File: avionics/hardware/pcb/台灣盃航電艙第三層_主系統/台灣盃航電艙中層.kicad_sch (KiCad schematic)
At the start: 54 parts, among them J2 Micro_SD_Card_Det2, J3 Conn_01x04_Pin, SW1 SW_SPST, U1 STM32F405VGT6, U2 BMI088, U3 BMP390L, U4 Connector, U5 H3LIS331DL, Y1 8MHz

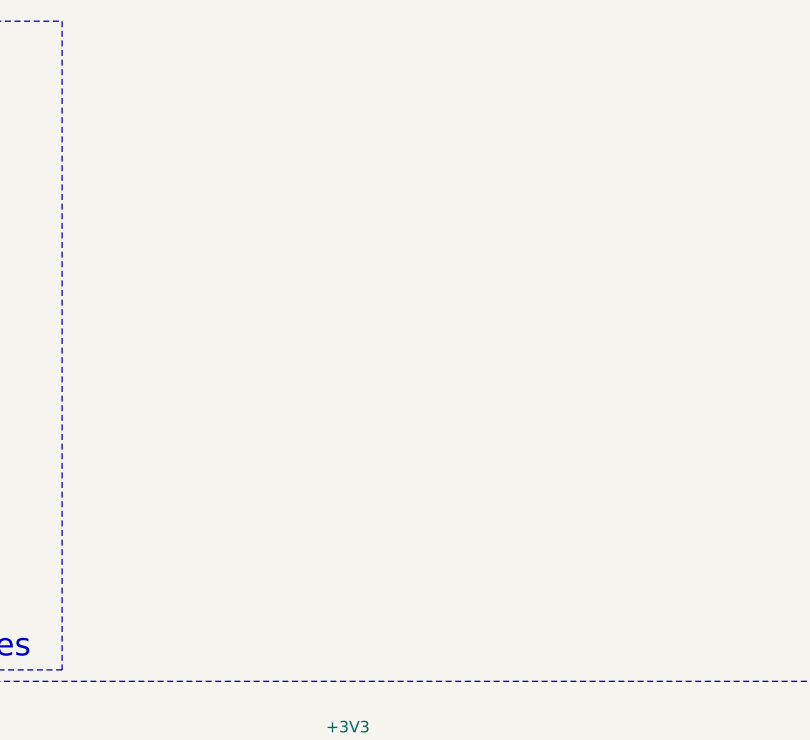
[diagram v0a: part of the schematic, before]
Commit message: 上傳新的連接器
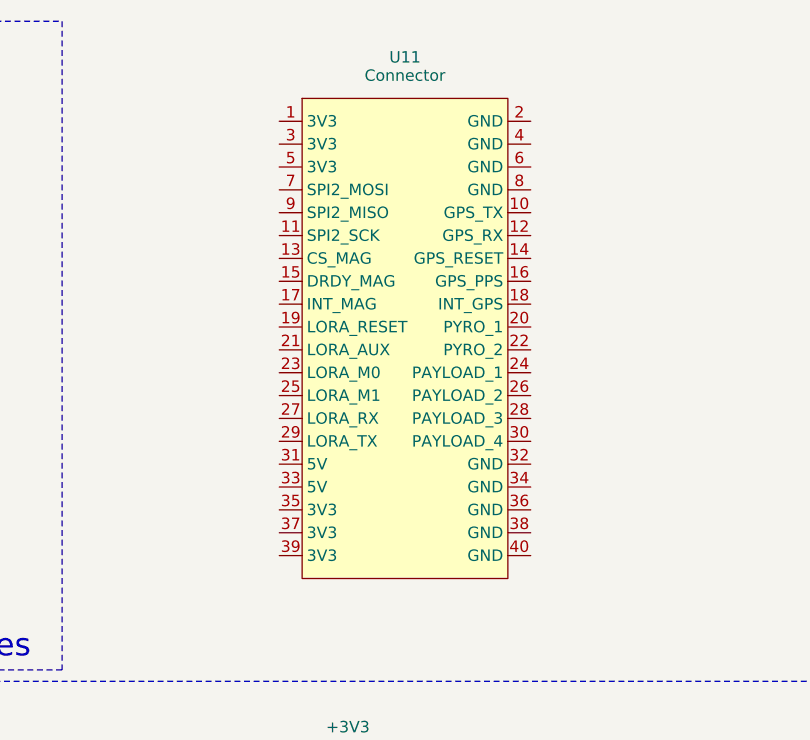
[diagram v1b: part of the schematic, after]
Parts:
- added U11: Connector, symbol MySymbol:2*20 PC104
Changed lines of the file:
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@@
+	)
+	(symbol
+		(lib_id "MySymbol:2*20 PC104")
+		(at 290.83 21.59 0)
+		(unit 1)
+		(exclude_from_sim no)
+		(in_bom yes)
+		(on_board yes)
+		(dnp no)
+		(property "Reference" "U11"
+			(at 290.83 18.288 0)
+			(effects
+				(font
+					(size 1.27 1.27)
+				)
+			)
+		)
+		(property "Value" "Connector"
+			(at 290.83 20.32 0)
+			(effects
+				(font
+					(size 1.27 1.27)
+				)
+			)
+		)
+		(property "Footprint" ""
+			(at 290.83 21.59 0)
+			(effects
+				(font
+					(size 1.27 1.27)
+				)
+				(hide yes)
+			)
+		)
+		(property "Datasheet" ""
+			(at 290.83 21.59 0)
+			(effects
+				(font
+					(size 1.27 1.27)
+				)
+				(hide yes)
+			)
+		)
+		(property "Description" ""
+			(at 290.83 21.59 0)
+			(effects
+				(font
+					(size 1.27 1.27)
+				)
+				(hide yes)
+			)
+		)
+		(pin "19"
+		)
+		(pin "39"
+		)
+		(pin "9"
+		)
+		(pin "15"
+		)
+		(pin "11"
+		)
+		(pin "7"
+		)
+		(pin "29"
+		)
+		(pin "31"
+		)
+		(pin "5"
+		)
+		(pin "4"
+		)
+		(pin "1"
+		)
+		(pin "21"
+		)
+		(pin "12"
+		)
+		(pin "27"
+		)
+		(pin "16"
+		)
+		(pin "20"
+		)
+		(pin "23"
+		)
+		(pin "13"
+		)
+		(pin "17"
+		)
+		(pin "3"
+		)
+		(pin "25"
+		)
+		(pin "33"
+		)
+		(pin "35"
+		)
+		(pin "37"
+		)
+		(pin "6"
+		)
+		(pin "2"
+		)
+		(pin "8"
+		)
+		(pin "14"
+		)
+		(pin "18"
+		)
+		(pin "10"
+		)
+		(pin "24"
+		)
+		(pin "26"
+		)
+		(pin "32"
+		)
+		(pin "34"
+		)
+		(pin "36"
+		)
+		(pin "38"
+		)
+		(pin "28"
+		)
+		(pin "30"
+		)
+		(pin "22"
+		)
+		(pin "40"
+		)
+		(instances
+			(project "台灣盃航電艙中層"
+				(path "/4789330c-02e1-4fa2-9a82-fdad6a603275"
+					(reference "U11")
+					(unit 1)
+				)
+			)
+		)
 	)
 	(symbol

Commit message: 將第一至三層連接器修改成PC104規格，第四層還未進行
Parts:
- removed C23, C26: 10u, Capacitor_SMD:C_0805_2012Metric, symbol Device:C
- removed C24, C27: 100n, Capacitor_SMD:C_0603_1608Metric, symbol Device:C
- removed U4: Connector, Connector_PinHeader_1.00mm:PinHeader_2x17_P1.00mm_Vertical, symbol MySymbol:2x16排針母座連接
- added C30, C32: 100n, Capacitor_SMD:C_0402_1005Metric, symbol Device:C
- added C31, C33: 10u, Capacitor_SMD:C_0603_1608Metric, symbol Device:C
- U11: footprint (none) -> Connector_PinHeader_2.54mm:PinHeader_2x20_P2.54mm_Vertical
- U3: footprint Bmp390l:XDCR_BMP390L -> BMP390L:XDCR_BMP390L
- Y1: value 8MHz -> 16MHz
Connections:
- net +3V3: now also U11.1 (3V3), U11.3 (3V3), U11.35 (3V3), U11.37 (3V3), U11.39 (3V3), U11.5 (3V3), C30.1, C31.1, C32.1, C33.1
- net CS_MAG: now also U11.13 (CS_MAG)
- net DRDY_MAG: now also U11.15 (DRDY_MAG)
- net GND: now also U11.2 (GND), U11.32 (GND), U11.34 (GND), U11.36 (GND), U11.38 (GND), U11.4 (GND), U11.40 (GND), U11.6 (GND), U11.8 (GND), C30.2, C31.2, C32.2, C33.2
- net GPS_PPS: now also U11.16 (GPS_PPS)
- net GPS_RESET: now also U11.14 (GPS_RESET)
- net GPS_RX: now also U11.12 (GPS_RX)
- net GPS_TX: now also U11.10 (GPS_TX)
- net INT_GPS: now also U11.18 (INT_GPS)
- net INT_MAG: now also U11.17 (INT_MAG)
- net LORA_AUX: now also U11.21 (LORA_AUX)
- net LORA_M0: now also U11.23 (LORA_M0)
- net LORA_M1: now also U11.25 (LORA_M1)
- net LORA_RESET: now also U11.19 (LORA_RESET)
- net LORA_RX: now also U11.27 (LORA_RX)
- net LORA_TX: now also U11.29 (LORA_TX)
- net PAYLOAD_1: now also U11.24 (PAYLOAD_1)
- net PAYLOAD_2: now also U11.26 (PAYLOAD_2)
- net PAYLOAD_3: now also U11.28 (PAYLOAD_3)
- net PAYLOAD_4: now also U11.30 (PAYLOAD_4)
- net PYRO1: now also U11.20 (PYRO_1)
- net PYRO2: now also U11.22 (PYRO_2)
- net SPI2_MISO: now also U11.9 (SPI2_MISO)
- net SPI2_MOSI: now also U11.7 (SPI2_MOSI)
- net SPI2_SCK: now also U11.11 (SPI2_SCK)
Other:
- moved on the sheet: U11
